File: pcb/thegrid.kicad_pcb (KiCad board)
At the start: 2 copper layers, 49.8 x 99.8 mm, 54 parts, among them P1 POWER, P10 CONN_2, P2 SHIFT_IN, P3 SHIFT_OUT, P4 CONN_2, P5 CONN_2, P6 CONN_2, P7 CONN_2, P8 CONN_2, P9 CONN_2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

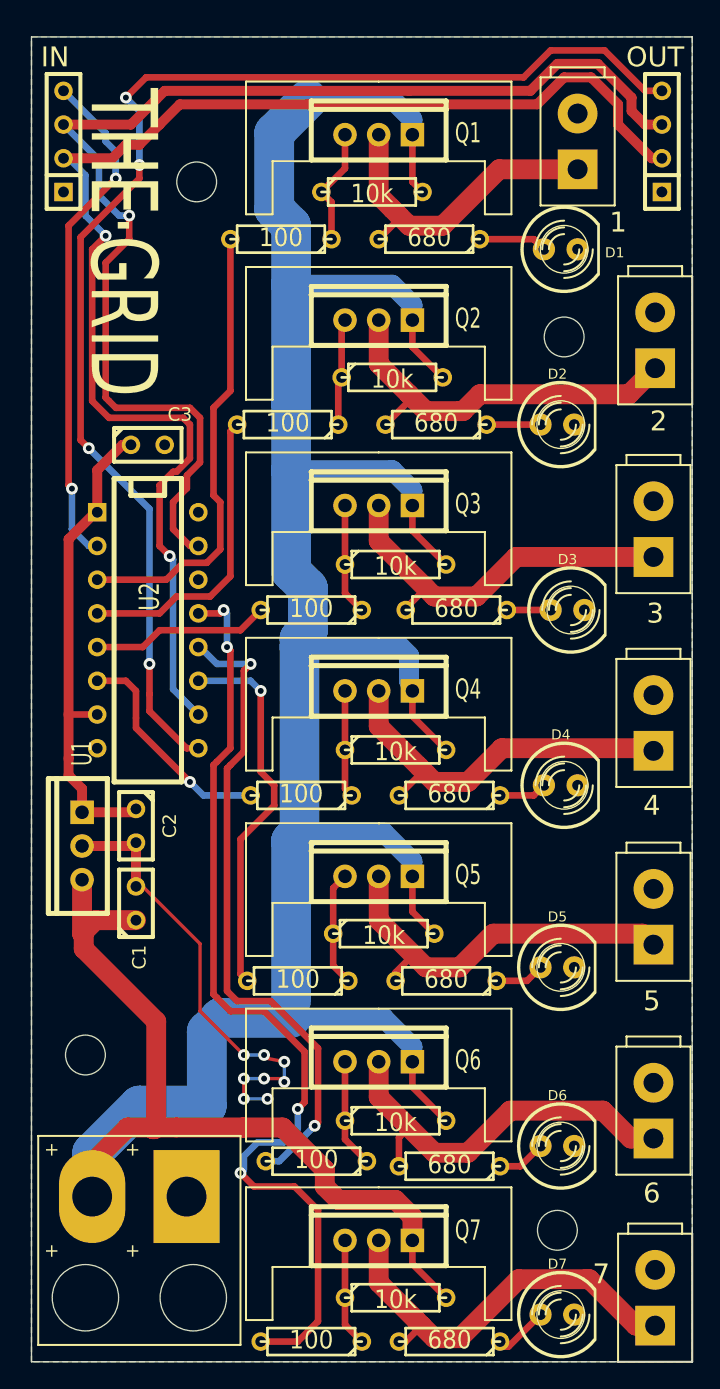
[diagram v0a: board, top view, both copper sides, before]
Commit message: Bumped up clearances
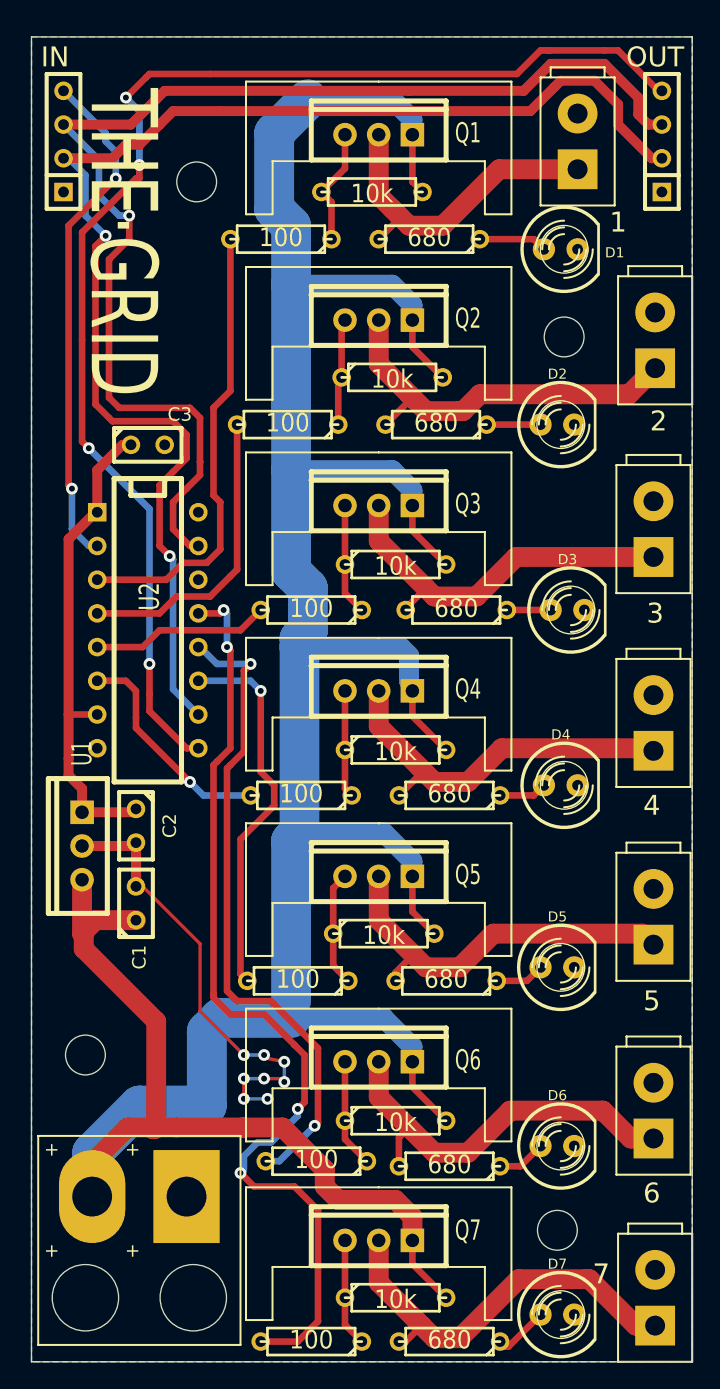
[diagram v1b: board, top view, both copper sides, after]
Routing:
- net Net-(P2-Pad2): track 103.5 -> 102.2 mm
- net Net-(R12-Pad2): track 73.0 -> 72.4 mm

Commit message: Bumped via size
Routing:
- net Net-(R12-Pad2): track 72.4 -> 70.7 mm, vias 4 -> 3

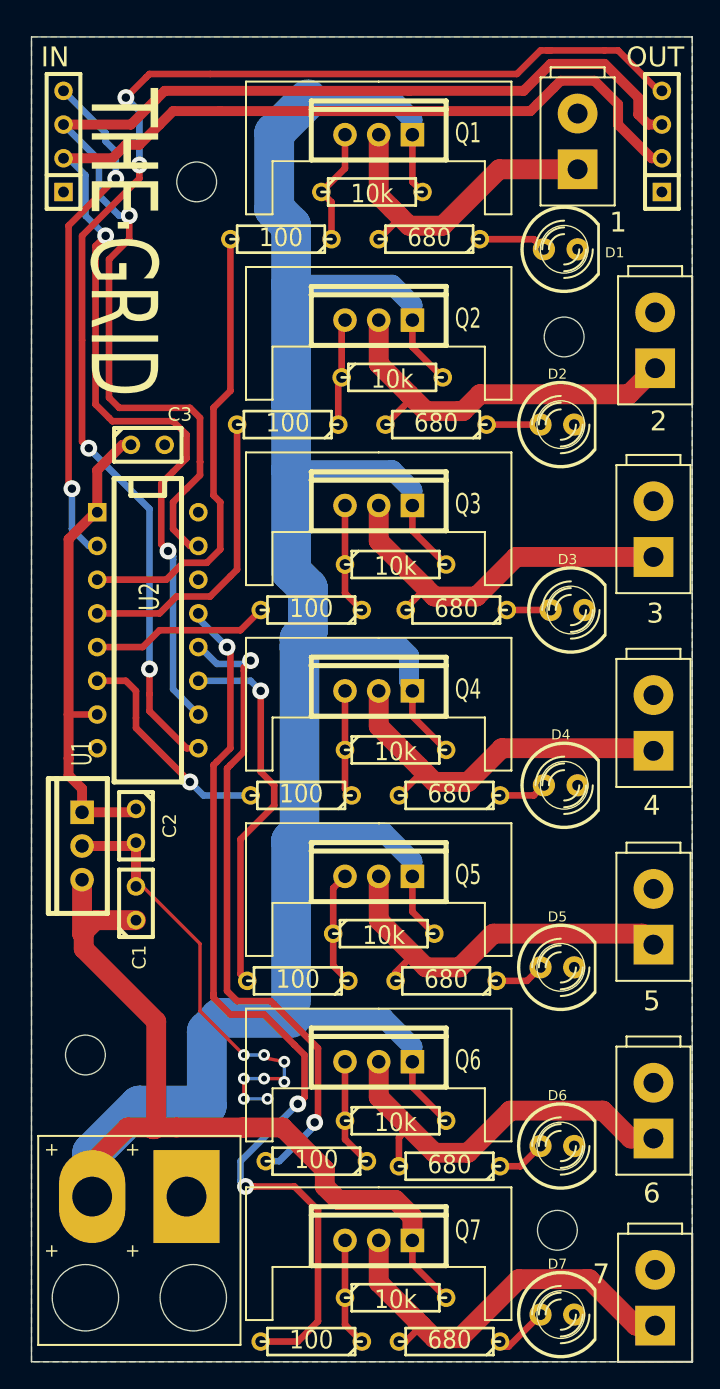
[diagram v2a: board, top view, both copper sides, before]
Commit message: Bumped thermal clearance spokes
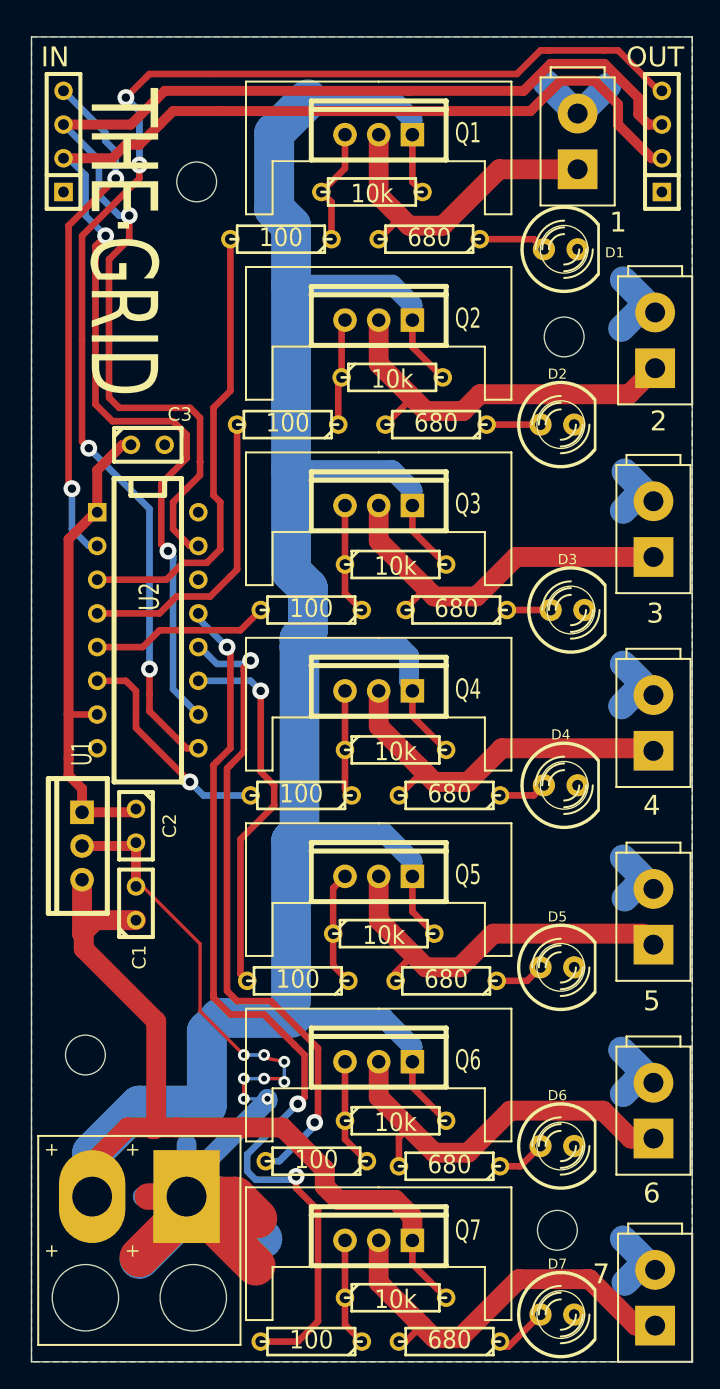
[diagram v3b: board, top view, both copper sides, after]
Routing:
- net GND: track 35.0 -> 130.4 mm

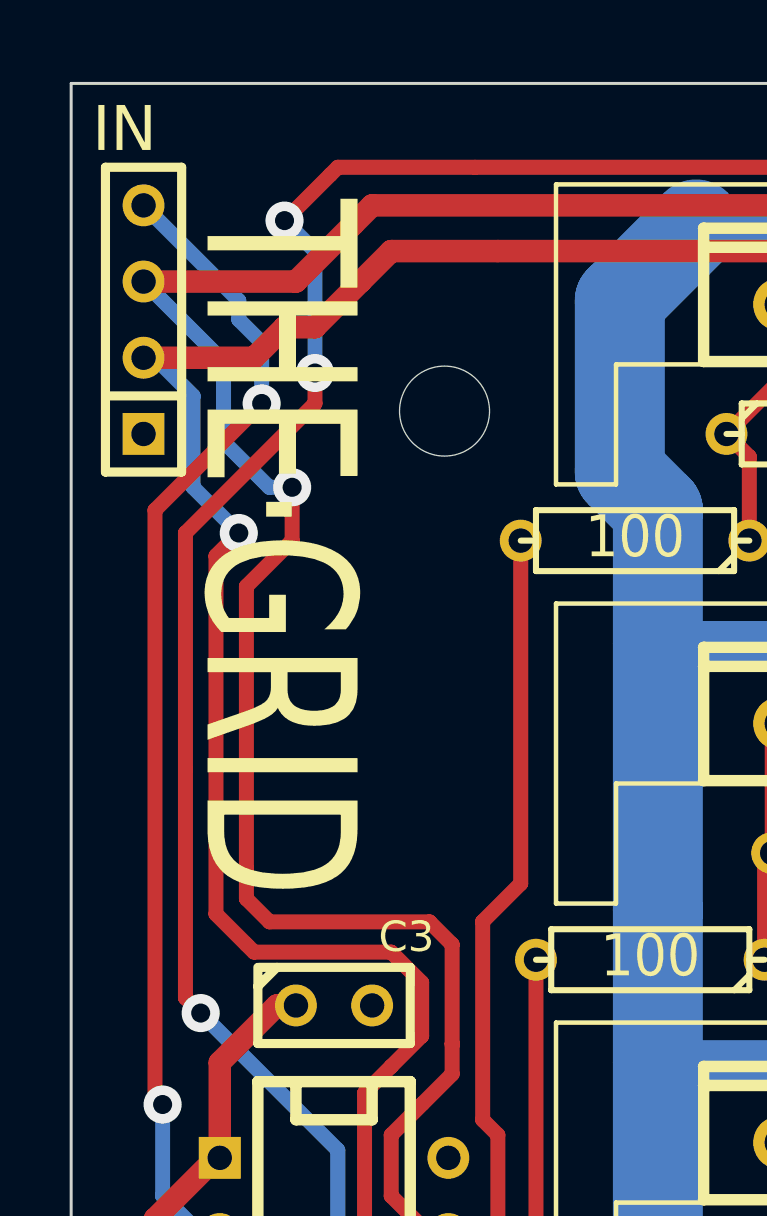
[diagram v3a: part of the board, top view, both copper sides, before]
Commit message: Moved silk off vias
Because Dirty apparently don't tent vias, and probably not ones this chunky!
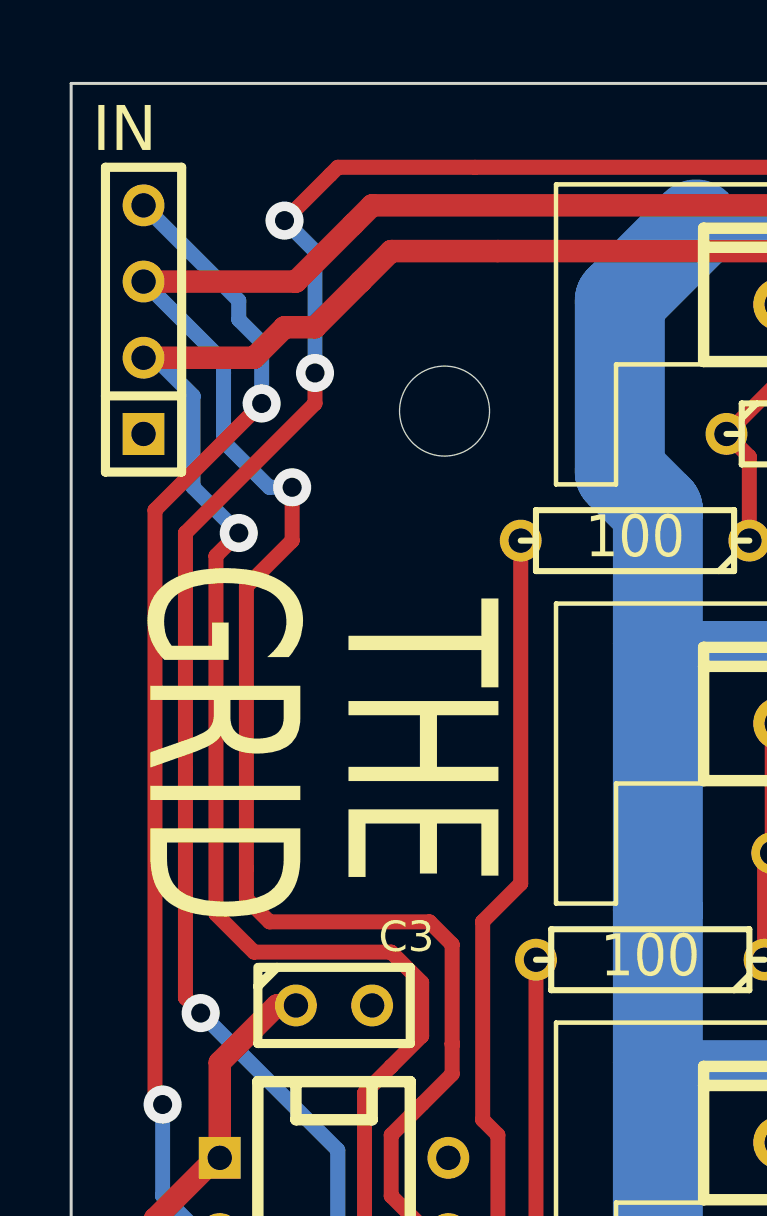
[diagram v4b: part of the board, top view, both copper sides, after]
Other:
- board text added: "GRID"
- board text added: "THE"
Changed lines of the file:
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@@
     (area 102.412073 18.189956 186.609447 119.70385)
     (thickness 1.6)
-    (drawings 18)
+    (drawings 19)
     (tracks 468)
     (zones 0)
@@
   (page A4)
   (layers
-    (0 F.Cu signal hide)
-    (31 B.Cu signal)
+    (0 F.Cu signal)
+    (31 B.Cu signal hide)
     (32 B.Adhes user hide)
     (33 F.Adhes user hide)
@@
     (35 F.Paste user hide)
     (36 B.SilkS user hide)
-    (37 F.SilkS user hide)
+    (37 F.SilkS user)
     (38 B.Mask user)
     (39 F.Mask user hide)
-    (40 Dwgs.User user hide)
-    (41 Cmts.User user hide)
+    (40 Dwgs.User user)
+    (41 Cmts.User user)
     (42 Eco1.User user hide)
     (43 Eco2.User user hide)
@@
     (pad_to_mask_clearance 0)
     (aux_axis_origin 0 0)
-    (visible_elements FFFFDF1F)
+    (visible_elements FFFFDF7F)
     (pcbplotparams
       (layerselection 0x010f0_80000001)
@@
     (pad 1 thru_hole circle (at 0 0) (size 2.99974 2.99974) (drill 2.99974) (layers))
   )
+  (gr_text GRID (at 126.365 40.767 270) (layer F.SilkS)
+    (effects (font (size 5 3.5) (thickness 0.75)))
+  )
   (gr_line (start 121.412 118.618) (end 171.196 118.618) (angle 90) (layer Edge.Cuts) (width 0.1))
   (gr_line (start 121.412 118.618) (end 121.412 18.796) (angle 90) (layer Edge.Cuts) (width 0.1))
@@
     (effects (font (size 1.5 1.5) (thickness 0.3)))
   )
-  (gr_text THE·GRID (at 128.27 34.29 270) (layer F.SilkS)
+  (gr_text THE (at 132.969 40.767 270) (layer F.SilkS)
     (effects (font (size 5 3.5) (thickness 0.75)))
   )
